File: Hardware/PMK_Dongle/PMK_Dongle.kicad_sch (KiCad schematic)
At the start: 31 parts, among them IC1 ESP32-S2FH4, J1 USB_A, U1 MIC5528-3.3YMT-T5, Y1 Crystal_GND24_Small

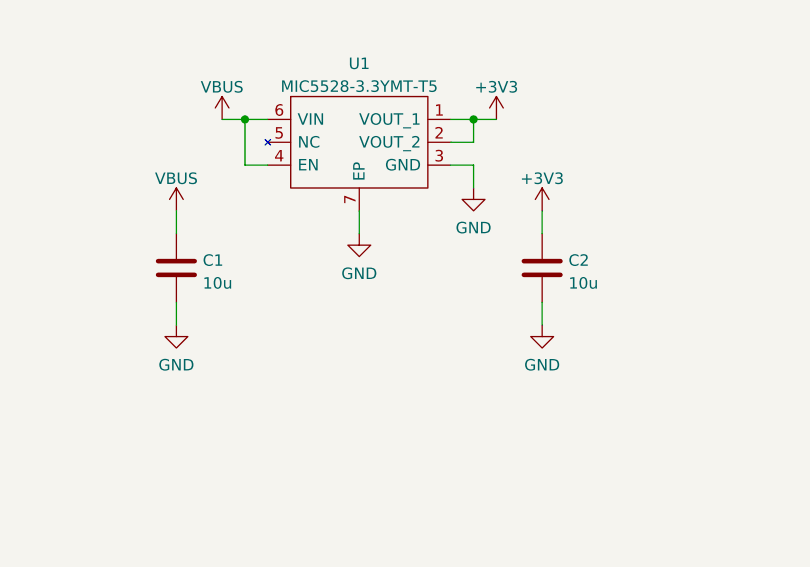
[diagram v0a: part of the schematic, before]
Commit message: added hierachic pages
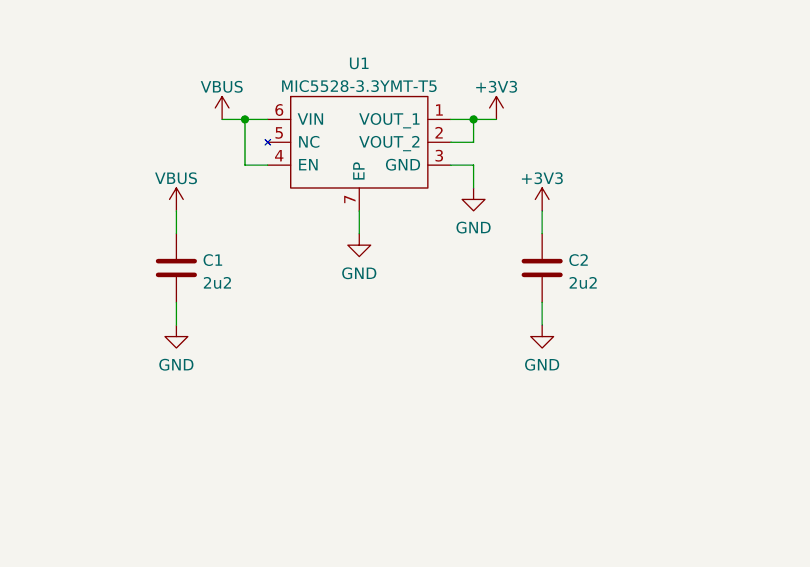
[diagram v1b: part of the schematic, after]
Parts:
- C1, C2: value 10u -> 2u2
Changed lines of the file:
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@@
       (effects (font (size 1.27 1.27)) (justify left))
     )
-    (property "Value" "10u" (id 1) (at 157.861 74.0922 0)
+    (property "Value" "2u2" (id 1) (at 157.861 74.0922 0)
       (effects (font (size 1.27 1.27)) (justify left))
     )
@@
       (effects (font (size 1.27 1.27)) (justify left))
     )
-    (property "Value" "10u" (id 1) (at 117.221 74.0922 0)
+    (property "Value" "2u2" (id 1) (at 117.221 74.0922 0)
       (effects (font (size 1.27 1.27)) (justify left))
     )
@@
     )
     (path "/fad526eb-f434-405a-8637-a318b4eb6d87"
-      (reference "C1") (unit 1) (value "10u") (footprint "Capacitor_SMD:C_0603_1608Metric")
+      (reference "C1") (unit 1) (value "2u2") (footprint "Capacitor_SMD:C_0603_1608Metric")
     )
     (path "/e7f5af2d-fef3-4584-b3e3-56f0c16949da"
-      (reference "C2") (unit 1) (value "10u") (footprint "Capacitor_SMD:C_0603_1608Metric")
+      (reference "C2") (unit 1) (value "2u2") (footprint "Capacitor_SMD:C_0603_1608Metric")
     )
     (path "/c218e4a4-9e59-473a-8d25-3c1d0f722ba6"
